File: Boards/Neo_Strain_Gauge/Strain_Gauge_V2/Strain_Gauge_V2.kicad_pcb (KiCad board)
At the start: 4 copper layers, 85 x 56 mm, 80 parts, among them J1 Screw_Terminal_01x03, J2 Screw_Terminal_01x03, J3 Screw_Terminal_01x03, J4 Screw_Terminal_01x03, J5 Conn_02x10_Counter_Clockwise, J6 Conn_02x12_Counter_Clockwise, J7 Conn_01x02, J8 USB_B_Micro, SW1 SW_DIP_x04, U1 W25Q128JVS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

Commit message: Update to latest code and board design. Include things like a purchase link for the DIP switch and closer to functional I2C.
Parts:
- SW1: footprint Button_Switch_SMD:SW_DIP_SPSTx04_Slide_Copal_CHS-04A_W5.08mm_P1.27mm_JPin -> Additional:SW4_1571983_4P_TEC
- moved R24 2.42 mm to (101.4, 133.2)
- moved R21 2.42 mm to (96.6, 133.2)
- moved R23 2.42 mm to (99.8, 133.1)
- moved R22 2.42 mm to (98.2, 133.2)
- moved SW1 1.44 mm to (107.5, 134.9)
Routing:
- net /Raspberry Pi/GPIO10: track 15.9 -> 18.7 mm
- net /Raspberry Pi/GPIO9: track 14.8 -> 17.5 mm
- net /Raspberry Pi/GPIO8: track 13.3 -> 15.7 mm
- net /Raspberry Pi/GPIO11: track 16.8 -> 18.9 mm
- net +3V3: track 257.3 -> 259.0 mm

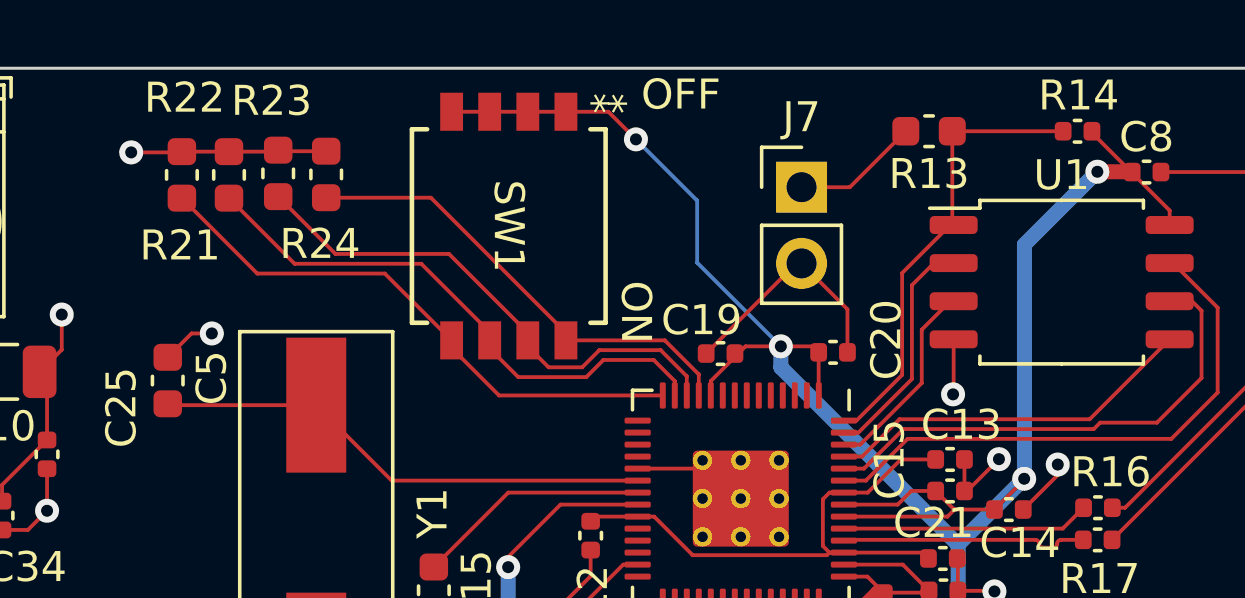
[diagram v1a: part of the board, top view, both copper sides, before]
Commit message: Updated strain gauge V2 to have a button
I need to update the button to be closer to ones we already have however.
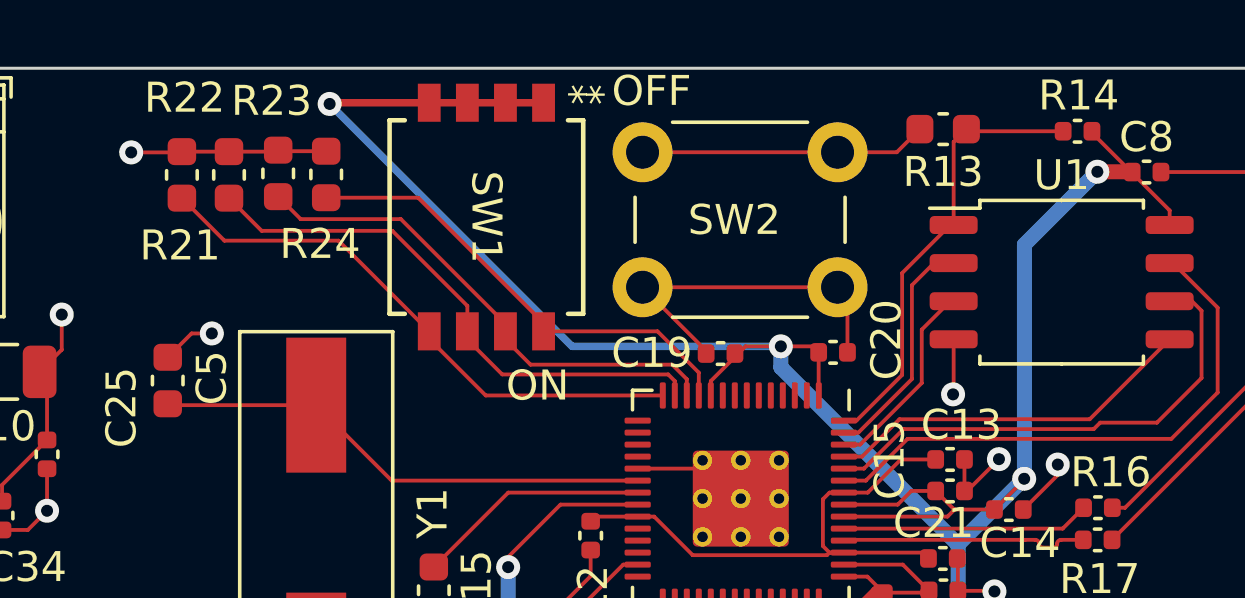
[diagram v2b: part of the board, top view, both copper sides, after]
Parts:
- removed J7: Conn_01x02, Connector_PinHeader_2.54mm:PinHeader_1x02_P2.54mm_Vertical
- added SW2: SW_Push, Button_Switch_THT:SW_PUSH_6mm_H4.3mm, F.Cu at (118.4, 136.9)
- R11, R12, R2, R3, R5, R6, R8, R9: value 350 -> 1000
- moved SW1 0.80 mm to (106.7, 134.6)
- moved R13 0.48 mm to (122.0, 131.7)
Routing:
- net +3V3: track 259.0 -> 269.1 mm
- net /Raspberry Pi/~{USB_BOOT}: track 4.25 -> 9.56 mm
- net GND: track 163.7 -> 166.7 mm

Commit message: Update footprint for part that we already have.
Technically footprint actually contains the name of the part here.
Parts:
- SW2: footprint Button_Switch_THT:SW_PUSH_6mm_H4.3mm -> Button_Switch_SMD:SW_SPST_B3U-1000P
- moved SW2 4.82 mm to (115.2, 133.4), turned to 90 degrees
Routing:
- net /Raspberry Pi/~{USB_BOOT}: track 9.56 -> 6.01 mm
- net GND: track 166.7 -> 166.0 mm, vias 33 -> 34

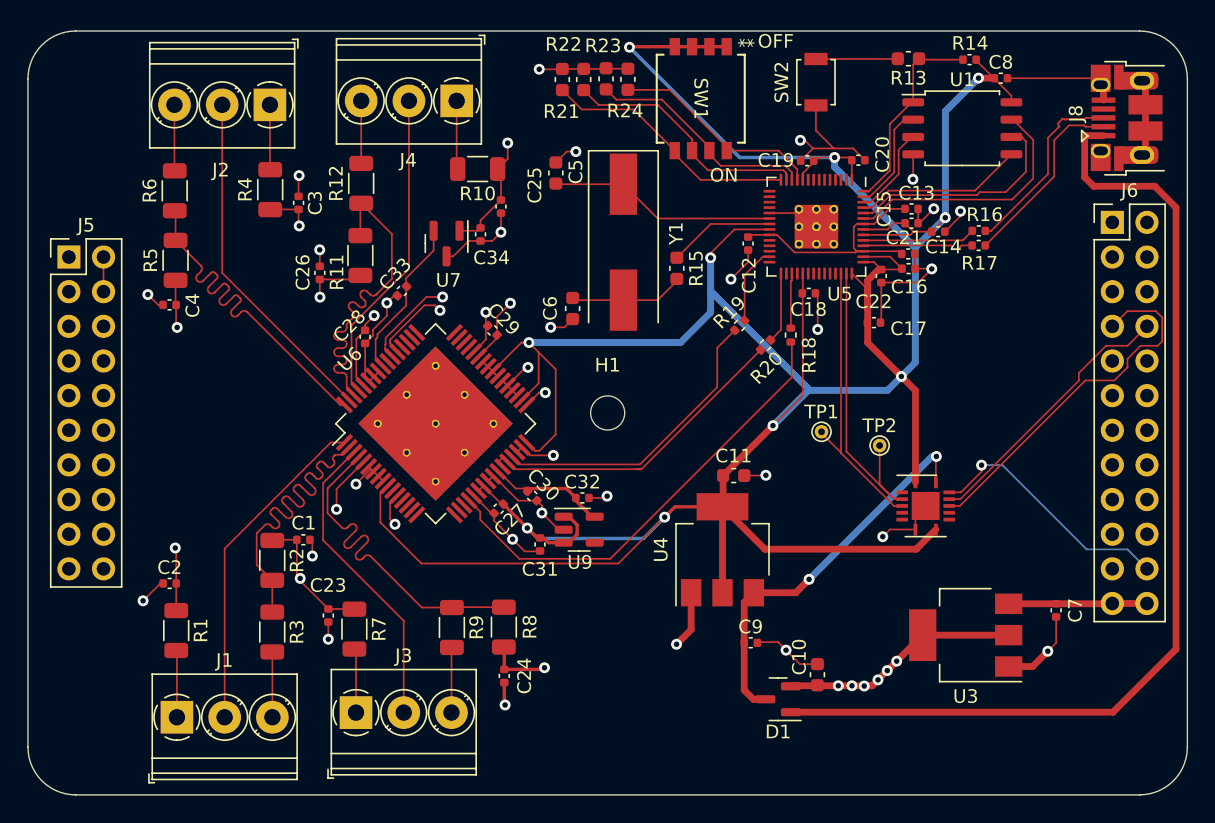
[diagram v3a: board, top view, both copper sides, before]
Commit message: Update board to use two voltage references
This will be a "demo" for a two-reference board, next I will most likely
design one with a differential instrumentation amplifier before
having a new board with 4 instrumentation amplifiers and a single-ended
ADC involved.
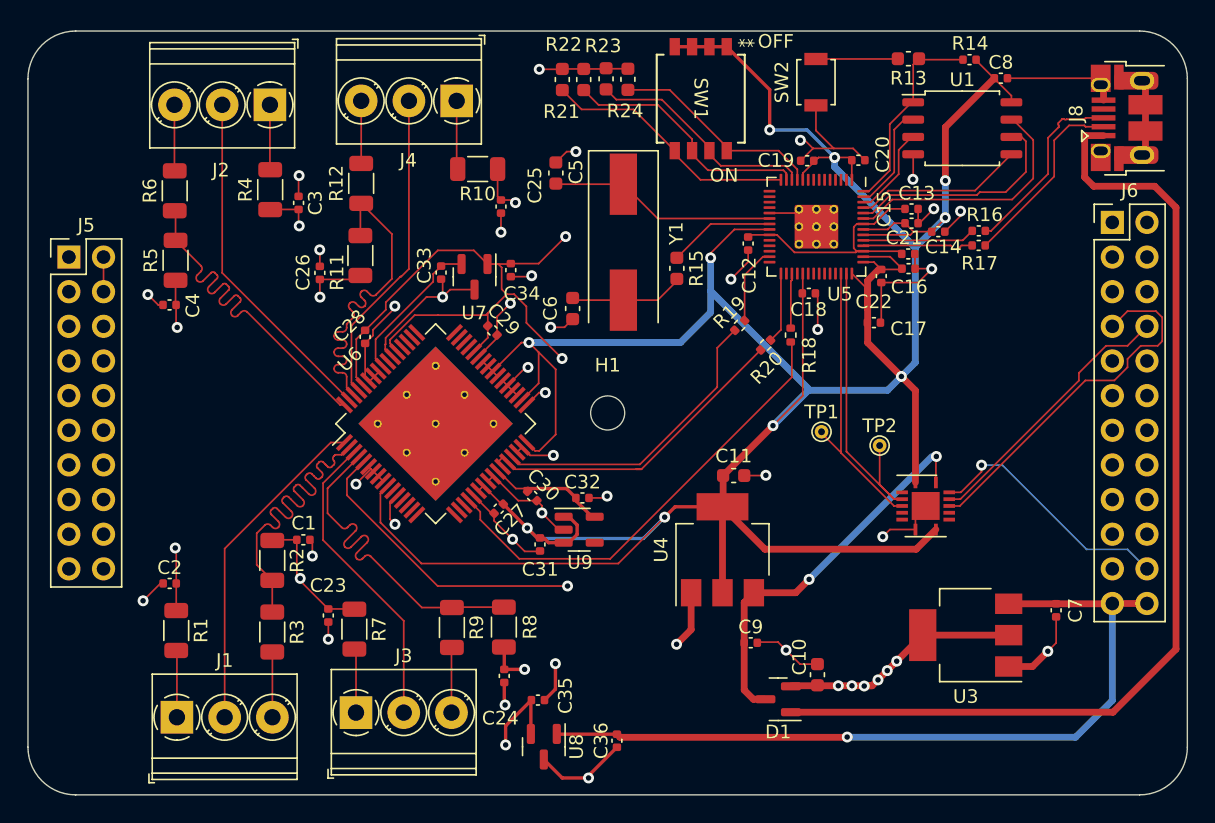
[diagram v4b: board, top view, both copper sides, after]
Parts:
- added C35: 10u, Capacitor_SMD:C_0402_1005Metric, F.Cu at (94.8, 178.7)
- added C36: 10u, Capacitor_SMD:C_0402_1005Metric, F.Cu at (100.6, 181.7)
- added U8: MAX6105, Package_TO_SOT_SMD:SOT-23, F.Cu at (95.2, 182.1)
- moved C34 3.43 mm to (92.8, 147.2)
- moved U7 3.19 mm to (90.2, 147.7)
- moved C33 3.17 mm to (87.7, 147.3), turned to -90 degrees
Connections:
- net /vcc renamed +12V
- C1 pad 2: +5V -> +5VA
- C2 pad 2: +5V -> +5VA
- C23 pad 2: +5V -> +5VA
- C24 pad 2: +5V -> +5VA
- C25 pad 2: +5V -> +5VA
- C26 pad 2: +5V -> +5VA
- C3 pad 2: +5V -> +5VA
- C4 pad 2: +5V -> +5VA
- R1 pad 1: +5V -> +5VA
- R10 pad 1: +5V -> +5VA
- R11 pad 1: +5V -> +5VA
- R2 pad 1: +5V -> +5VA
- R4 pad 1: +5V -> +5VA
- R5 pad 1: +5V -> +5VA
- R7 pad 1: +5V -> +5VA
- R8 pad 1: +5V -> +5VA
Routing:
- net +12V: track 10.1 -> 59.2 mm, vias 0 -> 1
- net +5VA: track 0.00 -> 38.8 mm, vias 0 -> 8
- net +5V: track 76.7 -> 86.8 mm, vias 17 -> 9
- net GND: track 166.0 -> 175.7 mm, vias 34 -> 37
- net +3V3: track 269.1 -> 259.7 mm
- net Net-(U6-VREFP): track 12.8 -> 11.1 mm
- added copper zone on In2.Cu, net +5VA
